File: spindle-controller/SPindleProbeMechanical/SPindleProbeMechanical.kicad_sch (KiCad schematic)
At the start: 20 parts, among them SW1 SPST Tilt Switch, U1 LM741, U2 DRV5055A1xDBZxQ1

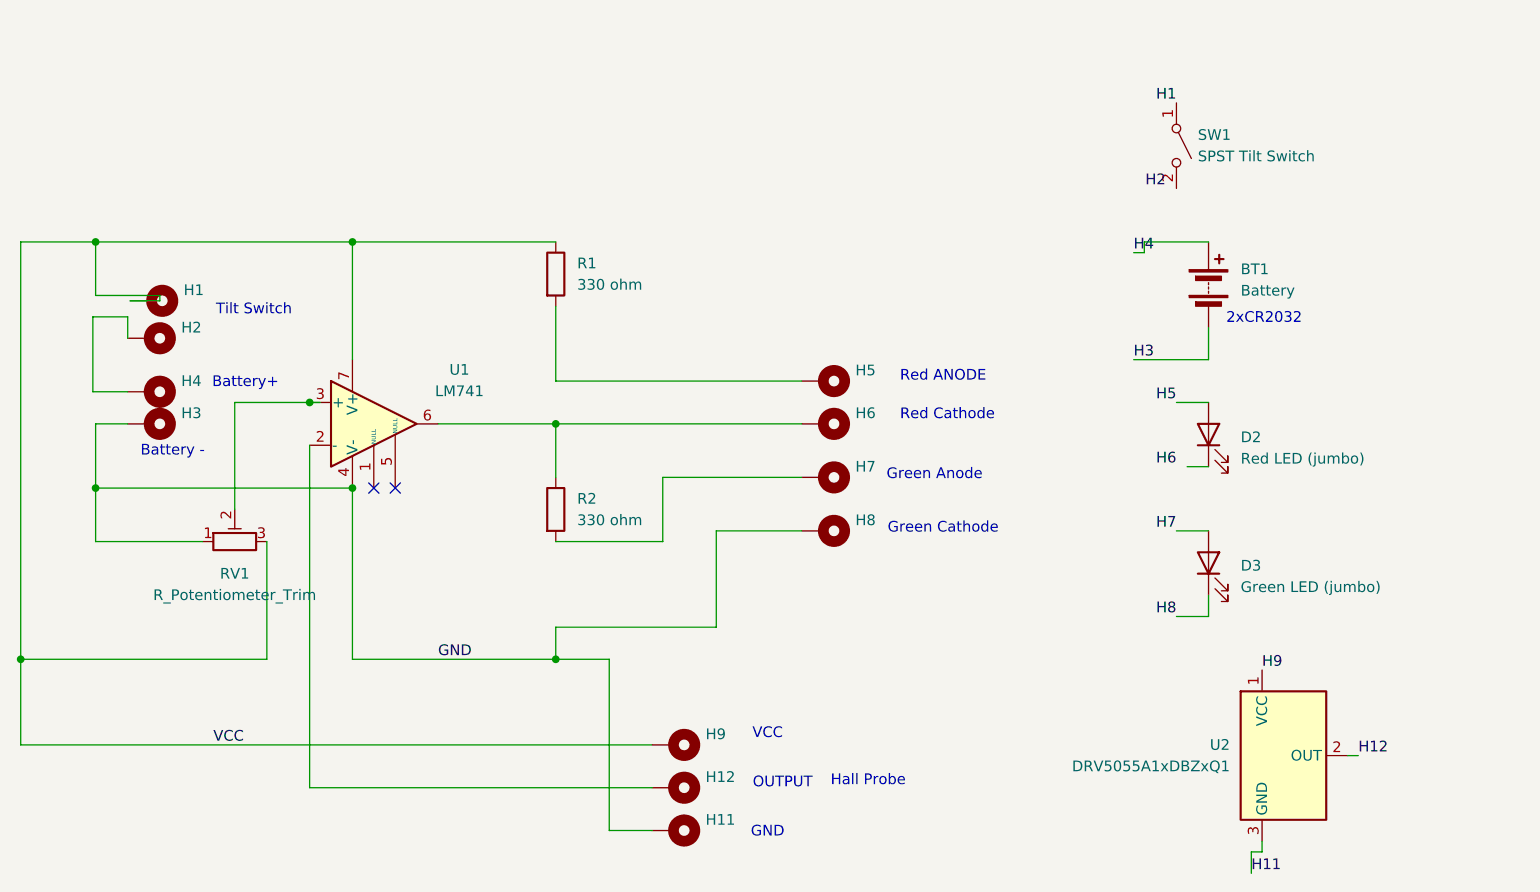
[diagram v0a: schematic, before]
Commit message: added the FOB circuit
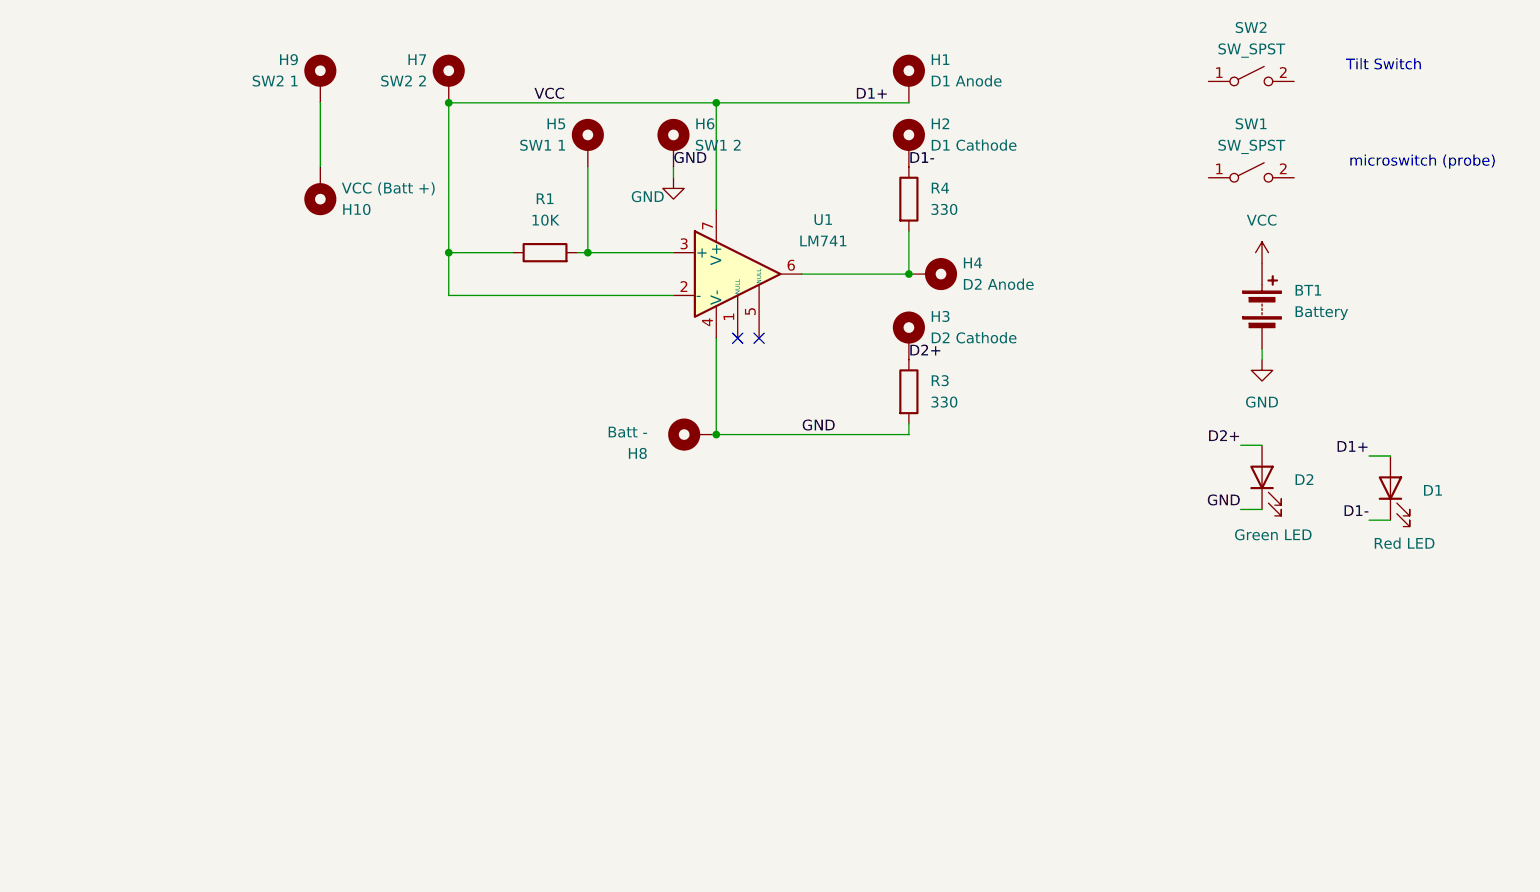
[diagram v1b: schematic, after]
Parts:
- removed D3: Green LED (jumbo), symbol Device:LED
- removed H11, H12: MountingHole_Pad, Connector_Wire:SolderWire-0.1sqmm_1x01_D0.4mm_OD1mm, symbol Mechanical:MountingHole_Pad
- removed R2: 330 ohm, Resistor_THT:R_Axial_DIN0207_L6.3mm_D2.5mm_P2.54mm_Vertical, symbol Device:R
- removed RV1: R_Potentiometer_Trim, Potentiometer_THT:Potentiometer_Bourns_3386W_Horizontal, symbol Device:R_Potentiometer_Trim
- removed U2: DRV5055A1xDBZxQ1, Package_TO_SOT_SMD:SOT-23, symbol Sensor_Magnetic:DRV5055A1xDBZxQ1
- added D1: Red LED, symbol Device:LED
- added H10: VCC (Batt +), Package_SO:TI_SO-PowerPAD-8, symbol Mechanical:MountingHole_Pad
- added R3, R4: 330, Resistor_THT:R_Axial_DIN0204_L3.6mm_D1.6mm_P1.90mm_Vertical, symbol Device:R
- added SW2: SW_SPST, Button_Switch_THT:SW_NKK_NR01, symbol Switch:SW_SPST
- D2: value Red LED (jumbo) -> Green LED
- H1: value MountingHole_Pad -> D1 Anode; footprint Connector_Wire:SolderWire-0.15sqmm_1x01_D0.5mm_OD1.5mm -> Package_SO:TI_SO-PowerPAD-8
- H2: value MountingHole_Pad -> D1 Cathode; footprint Connector_Wire:SolderWire-0.1sqmm_1x01_D0.4mm_OD1mm -> Package_SO:TI_SO-PowerPAD-8
- H3: value MountingHole_Pad -> D2 Cathode; footprint Connector_Wire:SolderWire-0.1sqmm_1x01_D0.4mm_OD1mm -> Package_SO:TI_SO-PowerPAD-8
- H4: value MountingHole_Pad -> D2 Anode; footprint Connector_Wire:SolderWire-0.1sqmm_1x01_D0.4mm_OD1mm -> Package_SO:TI_SO-PowerPAD-8
- H5: value MountingHole_Pad -> SW1 1; footprint Connector_Wire:SolderWire-0.1sqmm_1x01_D0.4mm_OD1mm -> Package_SO:TI_SO-PowerPAD-8
- H6: value MountingHole_Pad -> SW1 2; footprint Connector_Wire:SolderWire-0.1sqmm_1x01_D0.4mm_OD1mm -> Package_SO:TI_SO-PowerPAD-8
- H7: value MountingHole_Pad -> SW2 2; footprint Connector_Wire:SolderWire-0.1sqmm_1x01_D0.4mm_OD1mm -> Package_SO:TI_SO-PowerPAD-8
- H8: value MountingHole_Pad -> Batt -; footprint Connector_Wire:SolderWire-0.1sqmm_1x01_D0.4mm_OD1mm -> Package_SO:TI_SO-PowerPAD-8
- H9: value MountingHole_Pad -> SW2 1; footprint Connector_Wire:SolderWire-0.1sqmm_1x01_D0.4mm_OD1mm -> Package_SO:TI_SO-PowerPAD-8
- R1: value 330 ohm -> 10K; footprint Resistor_THT:R_Axial_DIN0207_L6.3mm_D2.5mm_P2.54mm_Vertical -> Resistor_THT:R_Axial_DIN0204_L3.6mm_D1.6mm_P1.90mm_Vertical
- SW1: value SPST Tilt Switch -> SW_SPST; footprint (none) -> Button_Switch_THT:SW_NKK_NR01
- U1: footprint Package_DIP:CERDIP-8_W7.62mm_SideBrazed_LongPads_Socket -> Package_DIP:DIP-8_W7.62mm
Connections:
- net H3 is gone; now on net GND: BT1.2 (-)
- net H4 is gone; now on net VCC: BT1.1 (+)
- net GND: now also D2.1 (K), H6.1, R3.2; no longer H3.1
- net VCC: now also H7.1, U1.2 (-), D1.2 (A); no longer H9.1
- net at U1.6: now also H4.1, R4.2; no longer H6.1
- net at H5.1, R1.2: now also U1.3 (+)
- net D1-: now reaches H2.1
- net D1-: now also D1.1 (K), R4.1; no longer H4.1
- net H1: no longer names the net of SW1.1 (A)
- net H5 renamed D2+
- net D2+: now also H3.1, R3.1
- new net: H10.1, H9.1
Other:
- note added: "microswitch (probe)"
- note removed: "2xCR2032"
- note removed: "Battery -"
- note removed: "Battery+"
- note removed: "GND"
- note removed: "Green Anode"
- note removed: "Green Cathode"
- note removed: "Hall Probe"
- note removed: "OUTPUT"
- note removed: "Red ANODE"
- note removed: "Red Cathode"
- note removed: "VCC"
